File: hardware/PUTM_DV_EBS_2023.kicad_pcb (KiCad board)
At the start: 4 copper layers, 97 x 70 mm, 148 parts, among them IC1 UCC2946DG4, J2 SWDIO_CONN, J6 IDC Connector, K1 FINDER-30.22, K2 FINDER-30.22, Q2 BSS123, Q3 BSS123, Q4 BSS123, U1 OPA365xxDBV, U10 74LVC1G08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

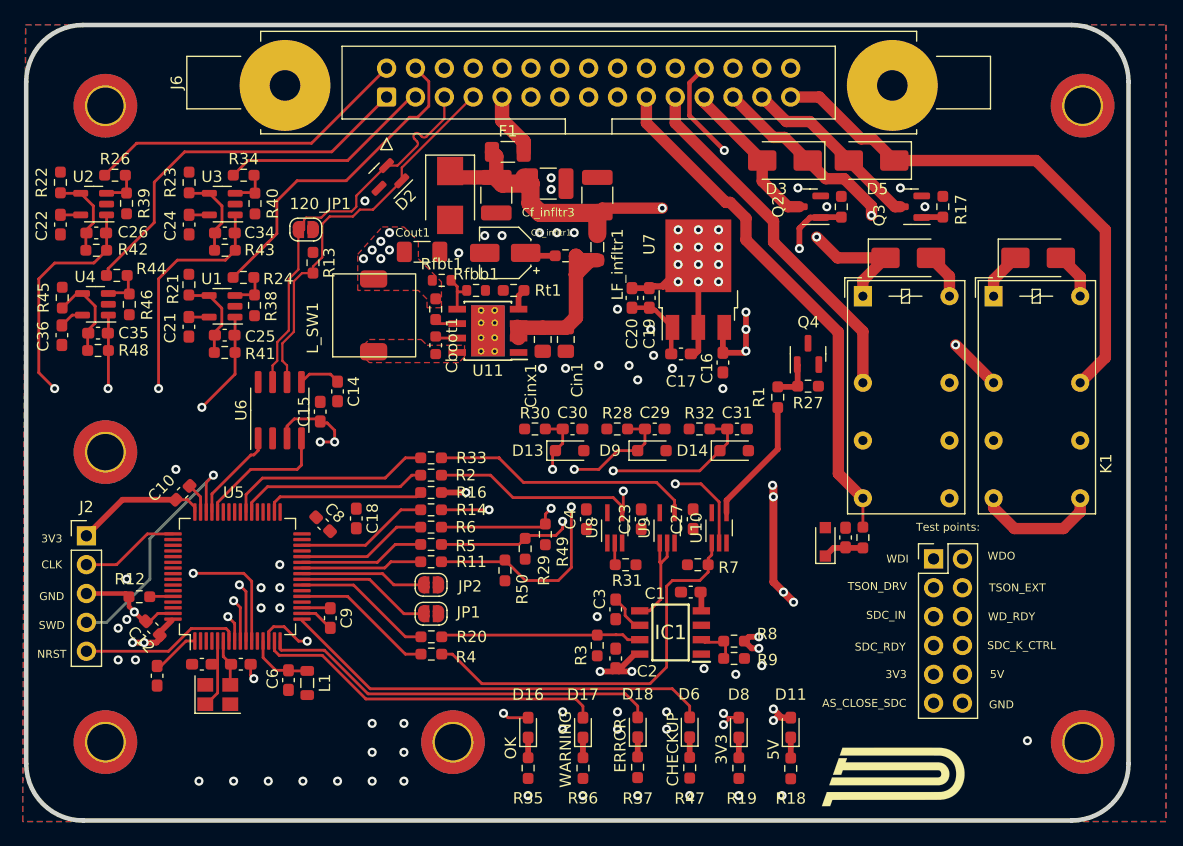
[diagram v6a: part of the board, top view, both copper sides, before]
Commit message: Adjust mounting holes to FBOX and BSPD
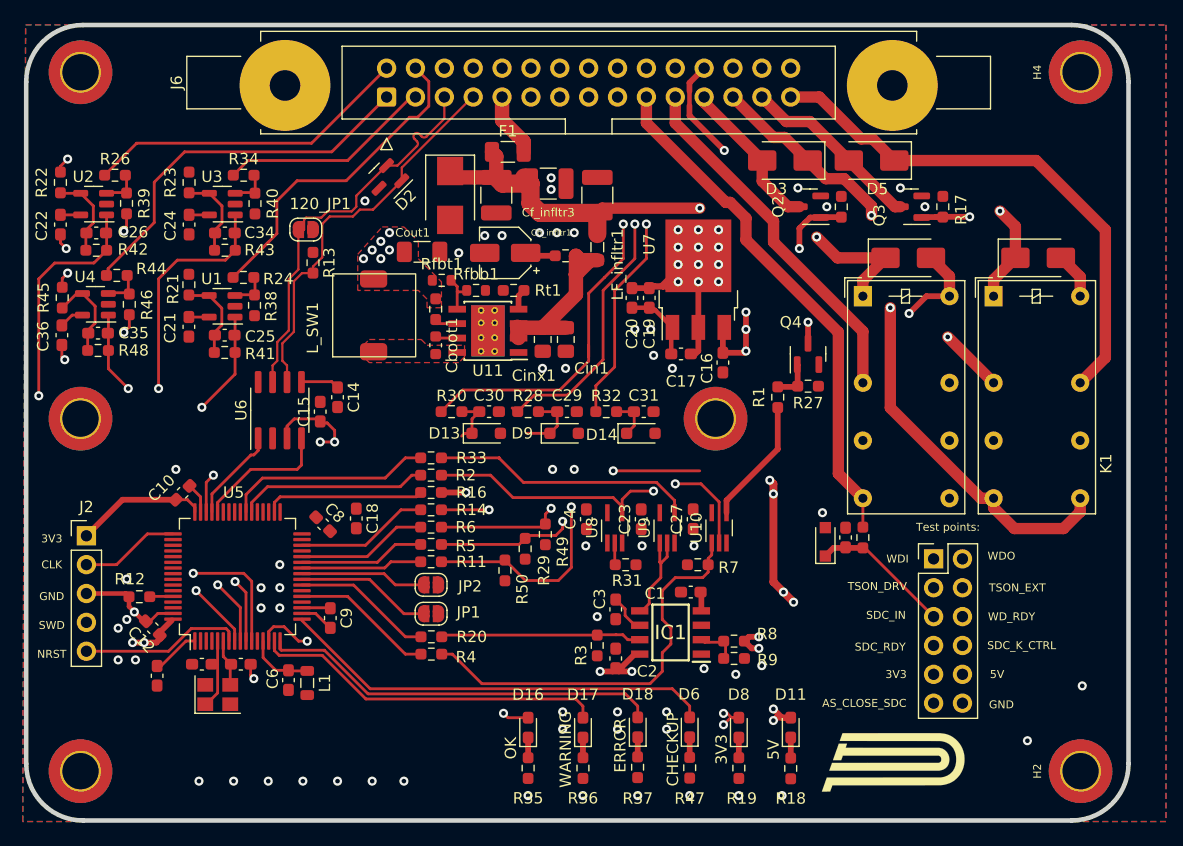
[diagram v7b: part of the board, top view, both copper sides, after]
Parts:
- removed H5, H6: MountingHole_3.2mm_M3_DIN965_Pad_TopBottom, MountingHole:MountingHole_3.2mm_M3_DIN965_Pad_TopBottom
- added H2: MountingHole_Pad, MountingHole:MountingHole_3.2mm_M3_DIN965_Pad_TopBottom, F.Cu at (185.8, 96.7)
- added H4: MountingHole_Pad, MountingHole:MountingHole_3.2mm_M3_DIN965_Pad_TopBottom, F.Cu at (185.8, 35.2)
- H1, H3: value MountingHole_3.2mm_M3_DIN965_Pad_TopBottom -> MountingHole_Pad
- moved H3 59.0 mm to (97.8, 35.2), turned to 90 degrees
- moved H1 58.6 mm to (97.8, 96.7), turned to 90 degrees
- moved H4 36.7 mm to (153.7, 65.6)
- moved C31 8.35 mm to (147.3, 65.0)
- moved D14 8.35 mm to (147.1, 66.9)
- moved R32 8.35 mm to (144.0, 65.0)
- moved R28 7.99 mm to (137.2, 65.0)
- moved C29 7.87 mm to (140.6, 65.0)
- moved D9 7.87 mm to (140.3, 66.9)
- moved C30 7.50 mm to (133.7, 65.0)
- moved R30 7.50 mm to (130.4, 65.0)
- moved D13 7.50 mm to (133.5, 66.9)
- moved H2 3.67 mm to (97.8, 65.6)
- moved PUTM_LOGO 1.28 mm to (168.9, 95.7)
- moved C14 0.51 mm to (120.4, 63.8)
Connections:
- J6 pad 10: AUX2 -> SPARE2
- J6 pad 12: AUX1 -> SPARE1
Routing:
- net LINE: track 20.1 -> 64.5 mm, vias 1 -> 2
- net Net-(Q3-G): track 35.2 -> 78.8 mm, vias 1 -> 2
- net DASH_TS_ON: track 0.00 -> 42.7 mm, vias 0 -> 1
- net TSMS: track 4.17 -> 42.2 mm, vias 0 -> 1
- net TS_ON_EXTERNAL: track 0.00 -> 36.0 mm, vias 0 -> 1
- net EBS_RESET _BUTTON: track 0.00 -> 30.6 mm, vias 0 -> 1
- net Net-(Q2-G): track 36.2 -> 64.6 mm
- net Net-(D12-A): track 4.05 -> 20.8 mm, vias 0 -> 2
- net GND: track 27.4 -> 36.5 mm, vias 59 -> 62
- net /Input Protection/SAFETY_SENSE_P: track 5.53 -> 14.3 mm
- net SWDIO: track 22.1 -> 30.3 mm
- net TS_ON_EXT_P: track 26.8 -> 22.8 mm
- net SAFETY_RESET_BUTT_P: track 37.7 -> 35.2 mm
- net Net-(#FLG02-pwr): track 15.9 -> 16.8 mm
- net VALVE_1_COIL_I: track 36.2 -> 37.0 mm
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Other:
- board text added: "J3"
